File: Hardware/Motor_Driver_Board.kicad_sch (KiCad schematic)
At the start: 36 parts, among them J1 POWER, J2 MOTOR, J3 LCD, SW1 ENCODER, U1 XL1509-5.0

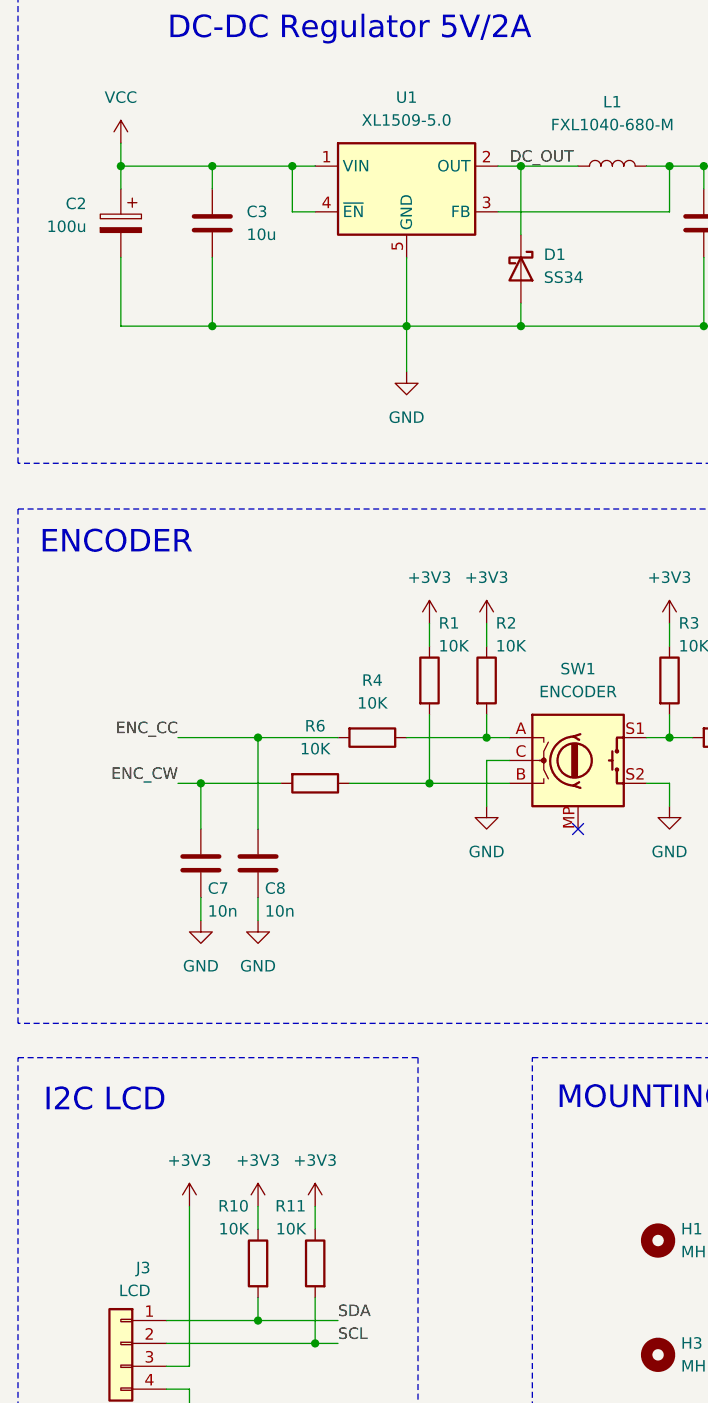
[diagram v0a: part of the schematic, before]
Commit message: Structure and software
Updated the project structure.
Added an initial software for the board.
Fixed minor errors on the PCB.
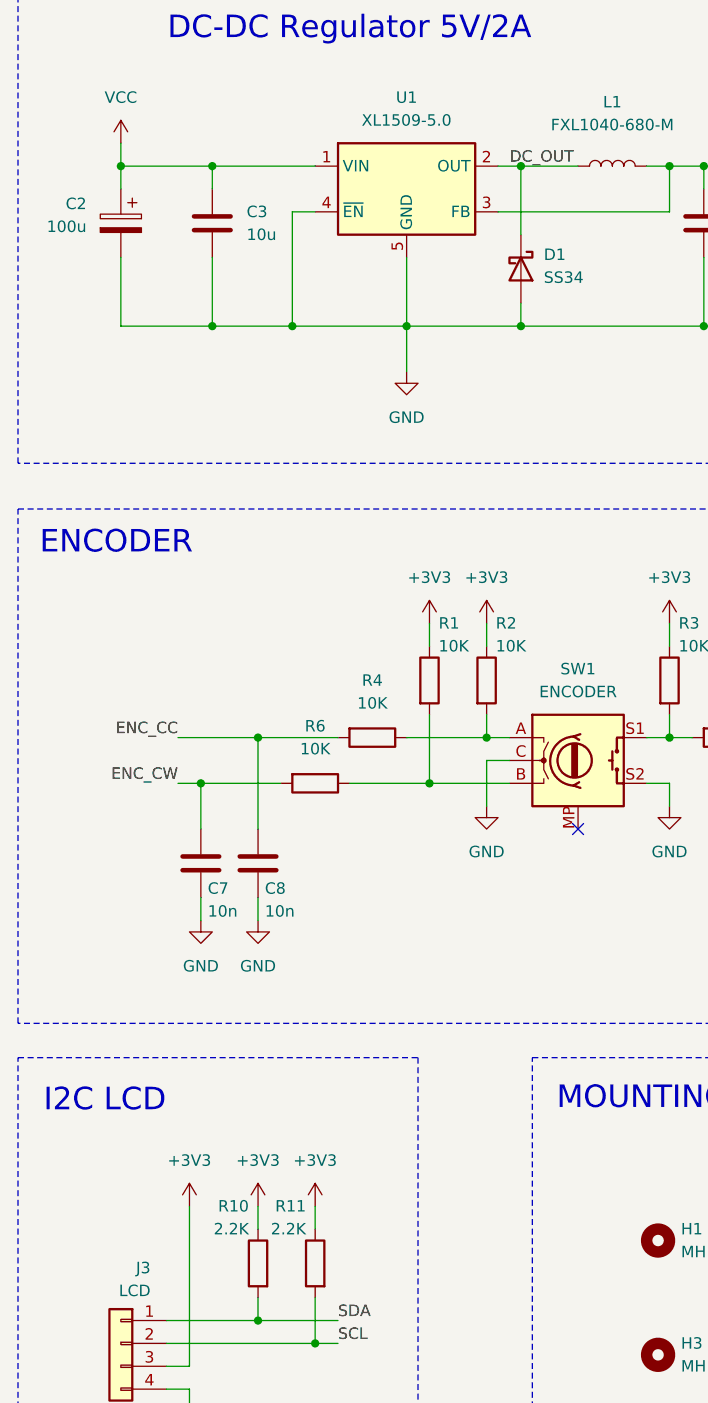
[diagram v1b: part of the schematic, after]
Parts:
- R10, R11: value 10K -> 2.2K
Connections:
- net GND: now also U1.4 (~{EN})
- net VCC: no longer U1.4 (~{EN})
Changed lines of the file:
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@@
 	)
 	(junction
-		(at 50.8 44.45)
-		(diameter 0)
-		(color 0 0 0 0)
-	)
-	(junction
 		(at 105.41 107.95)
 		(diameter 0)
@@
 	)
 	(junction
+		(at 50.8 62.23)
+		(diameter 0)
+		(color 0 0 0 0)
+	)
+	(junction
 		(at 96.52 62.23)
 		(diameter 0)
@@
 	(wire
 		(pts
+			(xy 50.8 49.53) (xy 50.8 62.23)
+		)
+		(stroke
+			(width 0)
+			(type default)
+		)
+	)
+	(wire
+		(pts
 			(xy 242.57 87.63) (xy 247.65 87.63)
 		)
@@
 	(wire
 		(pts
-			(xy 41.91 44.45) (xy 50.8 44.45)
+			(xy 41.91 44.45) (xy 53.34 44.45)
 		)
 		(stroke
@@
 	(wire
 		(pts
-			(xy 41.91 62.23) (xy 63.5 62.23)
+			(xy 41.91 62.23) (xy 50.8 62.23)
 		)
 		(stroke
@@
 	(wire
 		(pts
-			(xy 50.8 44.45) (xy 50.8 49.53)
-		)
-		(stroke
-			(width 0)
-			(type default)
-		)
-	)
-	(wire
-		(pts
 			(xy 96.52 62.23) (xy 96.52 54.61)
 		)
@@
 	(wire
 		(pts
-			(xy 50.8 44.45) (xy 53.34 44.45)
-		)
-		(stroke
-			(width 0)
-			(type default)
-		)
-	)
-	(wire
-		(pts
 			(xy 160.02 57.15) (xy 162.56 57.15)
 		)
@@
 	(wire
 		(pts
+			(xy 50.8 62.23) (xy 63.5 62.23)
+		)
+		(stroke
+			(width 0)
+			(type default)
+		)
+	)
+	(wire
+		(pts
 			(xy 138.43 91.44) (xy 140.97 91.44)
 		)
@@
 			)
 		)
-		(property "Value" "10K"
+		(property "Value" "2.2K"
 			(at 45.974 162.56 0)
 			(show_name no)
@@
 			)
 		)
-		(property "Value" "10K"
+		(property "Value" "2.2K"
 			(at 52.324 162.56 0)
 			(show_name no)
